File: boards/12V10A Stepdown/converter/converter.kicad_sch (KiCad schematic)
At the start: 27 parts, among them IC1 CSD17578Q3A, J1 TB005-762-02BE, J2 TB005-762-02BE, Q1 CSD17571Q2, U1 LM25145RGYR

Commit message: Whoops didn't save
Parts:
- 2.2uH: value L -> L1; footprint (none) -> 10A_LIbrary:IND_XAL7070_COC
- Cbst, Cvin: footprint (none) -> 10A_LIbrary:CAP_1608_TDK
- Ccomp1, Ccomp2, Css: footprint (none) -> 10A_LIbrary:G-155_MUR
- Ccomp3: footprint (none) -> 10A_LIbrary:CAPC1005X55N
- Cilim, Cvcc, Rvcc: footprint (none) -> 10A_LIbrary:CAP_06031U0R5BAT2A
- Cin: footprint (none) -> 10A_LIbrary:CAP_MSAS32-M_TAY
- Cout: footprint (none) -> 10A_LIbrary:PCAP_SVP_B6_PAN
- M1: renamed from IC1; footprint CSD17578Q3A:TRANS_CSD18543Q3A -> 10A_LIbrary:DNH0008A
- M2: renamed from Q1; footprint CSD17571Q2:TRANS_CSD17571Q2 -> 10A_LIbrary:DQK0006C
- Rcomp2, Rfbb, Ruv1, Rvin: footprint (none) -> 10A_LIbrary:RC0402N_VIS
- Rfbt, Rpgood: footprint (none) -> 10A_LIbrary:RC0603N_YAG
- Rilim, Rt: footprint (none) -> 10A_LIbrary:RES_CRCW_0402
- Ruv2: footprint (none) -> 10A_LIbrary:RES_CRCW_0603
- U1: footprint LM25145RGYR:IC_LM25145RGYR -> 10A_LIbrary:RGY0020B
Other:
- moved on the sheet: 2.2uH, Cbst, Ccomp1, Ccomp2, Ccomp3, Cilim, Cin, Cout, Css, Cvcc, Cvin, J1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

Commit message: PCB schematic done with footprints
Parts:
- J1, J2: footprint TB005-762-02BE:CUI_TB005-762-02BE -> 10A_LIbrary:TB005-762-02BE_CUD
- Rcomp1: footprint (none) -> 10A_LIbrary:RES_CRCW_0402
- renumbered 2.2uH to 2.2uH1, Cbst to Cbst1, Cilim to Cilim1, Cin to Cin1, Cout to Cout1, Css to Css1, Cvcc to Cvcc1, Cvin to Cvin1, Rfbb to Rfbb1, Rfbt to Rfbt1, Rilim to Rilim1, Rpgood to Rpgood1, Rt to Rt1, Rvcc to Rvcc1, Rvin to Rvin1
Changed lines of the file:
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@@
 		(dnp no)
 		(fields_autoplaced yes)
-		(property "Reference" "Cilim"
+		(property "Reference" "Cilim1"
 			(at 162.56 120.6499 0)
 			(effects
@@
 			(project "converter"
 				(path "/1513ce43-e5f2-482b-99a2-cdd75b9aa1c1"
-					(reference "Cilim")
+					(reference "Cilim1")
 					(unit 1)
 				)
@@
 			)
 		)
-		(property "Footprint" ""
+		(property "Footprint" "10A_LIbrary:RES_CRCW_0402"
 			(at 189.484 82.804 90)
 			(effects
@@
 		(dnp no)
 		(fields_autoplaced yes)
-		(property "Reference" "Rfbb"
+		(property "Reference" "Rfbb1"
 			(at 214.63 130.8099 0)
 			(effects
@@
 			(project "converter"
 				(path "/1513ce43-e5f2-482b-99a2-cdd75b9aa1c1"
-					(reference "Rfbb")
+					(reference "Rfbb1")
 					(unit 1)
 				)
@@
 		(dnp no)
 		(fields_autoplaced yes)
-		(property "Reference" "Cvin"
+		(property "Reference" "Cvin1"
 			(at 82.55 69.8499 0)
 			(effects
@@
 			(project "converter"
 				(path "/1513ce43-e5f2-482b-99a2-cdd75b9aa1c1"
-					(reference "Cvin")
+					(reference "Cvin1")
 					(unit 1)
 				)
@@
 			)
 		)
-		(property "Footprint" "TB005-762-02BE:CUI_TB005-762-02BE"
+		(property "Footprint" "10A_LIbrary:TB005-762-02BE_CUD"
 			(at 252.73 114.3 0)
 			(effects
@@
 		(dnp no)
 		(fields_autoplaced yes)
-		(property "Reference" "Rpgood"
+		(property "Reference" "Rpgood1"
 			(at 139.7 99.0599 0)
 			(effects
@@
 			(project "converter"
 				(path "/1513ce43-e5f2-482b-99a2-cdd75b9aa1c1"
-					(reference "Rpgood")
+					(reference "Rpgood1")
 					(unit 1)
 				)
@@
 		(dnp no)
 		(fields_autoplaced yes)
-		(property "Reference" "2.2uH"
+		(property "Reference" "2.2uH1"
 			(at 168.91 90.17 90)
 			(effects
@@
 			(project "converter"
 				(path "/1513ce43-e5f2-482b-99a2-cdd75b9aa1c1"
-					(reference "2.2uH")
+					(reference "2.2uH1")
 					(unit 1)
 				)
@@
 		(dnp no)
 		(fields_autoplaced yes)
-		(property "Reference" "Cin"
+		(property "Reference" "Cin1"
 			(at 52.07 76.1999 0)
 			(effects
@@
 			(project "converter"
 				(path "/1513ce43-e5f2-482b-99a2-cdd75b9aa1c1"
-					(reference "Cin")
+					(reference "Cin1")
 					(unit 1)
 				)
@@
 		(dnp no)
 		(fields_autoplaced yes)
-		(property "Reference" "Rt"
+		(property "Reference" "Rt1"
 			(at 62.23 104.1399 0)
 			(effects
@@
 			(project "converter"
 				(path "/1513ce43-e5f2-482b-99a2-cdd75b9aa1c1"
-					(reference "Rt")
+					(reference "Rt1")
 					(unit 1)
 				)
@@
 		(dnp no)
 		(fields_autoplaced yes)
-		(property "Reference" "Cvcc"
+		(property "Reference" "Cvcc1"
 			(at 147.32 120.6499 0)
 			(effects
@@
 			(project "converter"
 				(path "/1513ce43-e5f2-482b-99a2-cdd75b9aa1c1"
-					(reference "Cvcc")
+					(reference "Cvcc1")
 					(unit 1)
 				)
@@
 		(dnp no)
 		(fields_autoplaced yes)
-		(property "Reference" "Css"
+		(property "Reference" "Css1"
 			(at 74.93 104.1399 0)
 			(effects
@@
 			(project "converter"
 				(path "/1513ce43-e5f2-482b-99a2-cdd75b9aa1c1"
-					(reference "Css")
+					(reference "Css1")
 					(unit 1)
 				)
@@
 		(dnp no)
 		(fields_autoplaced yes)
-		(property "Reference" "Cout"
+		(property "Reference" "Cout1"
 			(at 234.95 106.2481 0)
 			(effects
@@
 			(project "converter"
 				(path "/1513ce43-e5f2-482b-99a2-cdd75b9aa1c1"
-					(reference "Cout")
+					(reference "Cout1")
 					(unit 1)
 				)
@@
 		(dnp no)
 		(fields_autoplaced yes)
-		(property "Reference" "Rvin"
+		(property "Reference" "Rvin1"
 			(at 81.28 52.0699 0)
 			(effects
@@
 			(project "converter"
 				(path "/1513ce43-e5f2-482b-99a2-cdd75b9aa1c1"
-					(reference "Rvin")
+					(reference "Rvin1")
 					(unit 1)
 				)
@@
 		(dnp no)
 		(fields_autoplaced yes)
-		(property "Reference" "Rvcc"
+		(property "Reference" "Rvcc1"
 			(at 152.4 99.0599 0)
 			(effects
@@
 			(project "converter"
 				(path "/1513ce43-e5f2-482b-99a2-cdd75b9aa1c1"
-					(reference "Rvcc")
+					(reference "Rvcc1")
 					(unit 1)
 				)
@@
 		(dnp no)
 		(fields_autoplaced yes)
-		(property "Reference" "Cbst"
+		(property "Reference" "Cbst1"
 			(at 134.62 81.28 90)
 			(effects
@@
 			(project "converter"
 				(path "/1513ce43-e5f2-482b-99a2-cdd75b9aa1c1"
-					(reference "Cbst")
+					(reference "Cbst1")
 					(unit 1)
 				)
@@
 			)
 		)
-		(property "Footprint" "TB005-762-02BE:CUI_TB005-762-02BE"
+		(property "Footprint" "10A_LIbrary:TB005-762-02BE_CUD"
 			(at 39.37 60.96 0)
 			(effects
@@
 		(dnp no)
 		(fields_autoplaced yes)
-		(property "Reference" "Rfbt"
+		(property "Reference" "Rfbt1"
 			(at 214.63 100.3299 0)
 			(effects
@@
 			(project "converter"
 				(path "/1513ce43-e5f2-482b-99a2-cdd75b9aa1c1"
-					(reference "Rfbt")
+					(reference "Rfbt1")
 					(unit 1)
 				)
@@
 		(on_board yes)
 		(dnp no)
-		(property "Reference" "Rilim"
+		(property "Reference" "Rilim1"
 			(at 165.1 82.5499 0)
 			(effects
@@
 			(project "converter"
 				(path "/1513ce43-e5f2-482b-99a2-cdd75b9aa1c1"
-					(reference "Rilim")
-					(unit 1)
-				)
+					(reference "Rilim1")
+					(unit 1)
+				)

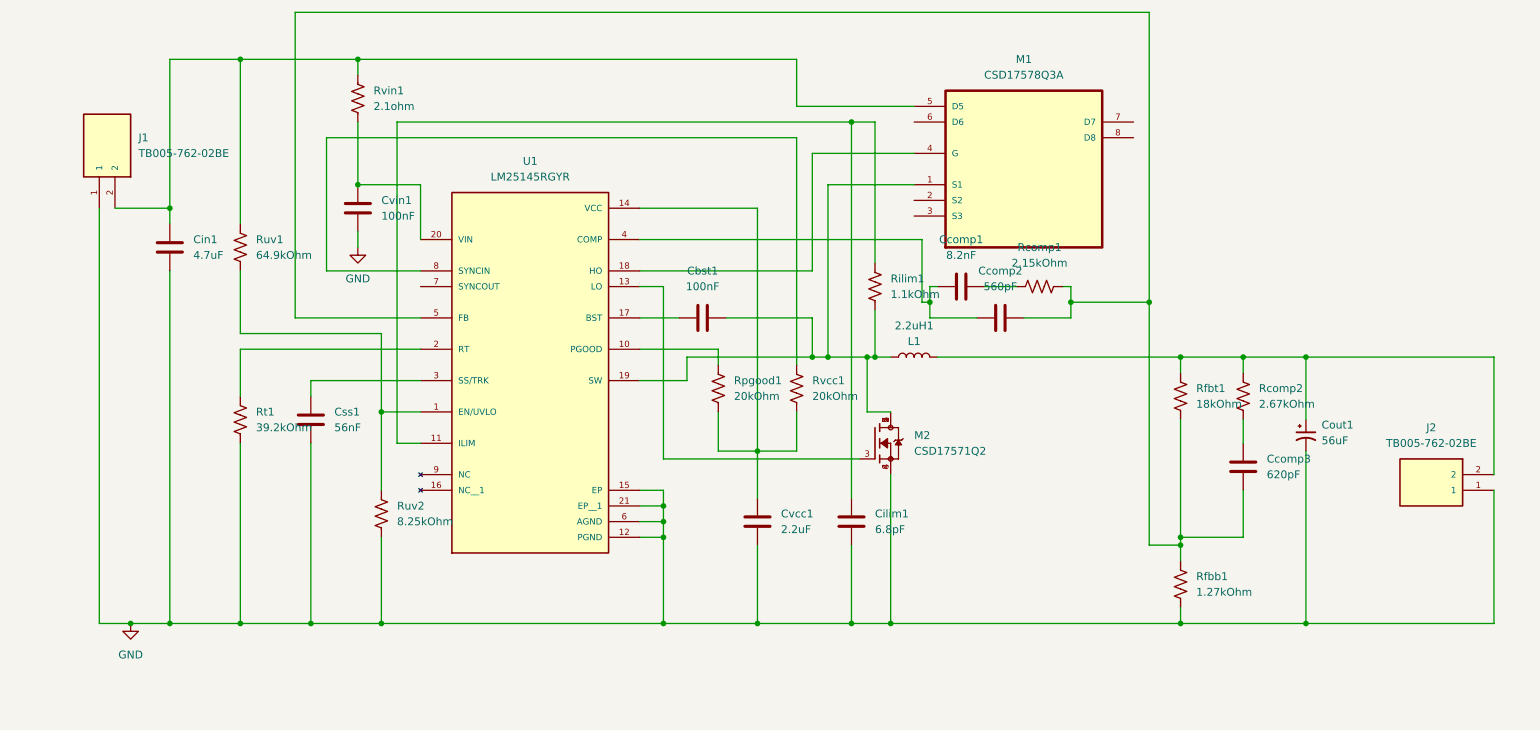
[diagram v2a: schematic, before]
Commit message: iris silkscreen stuff for 20a board
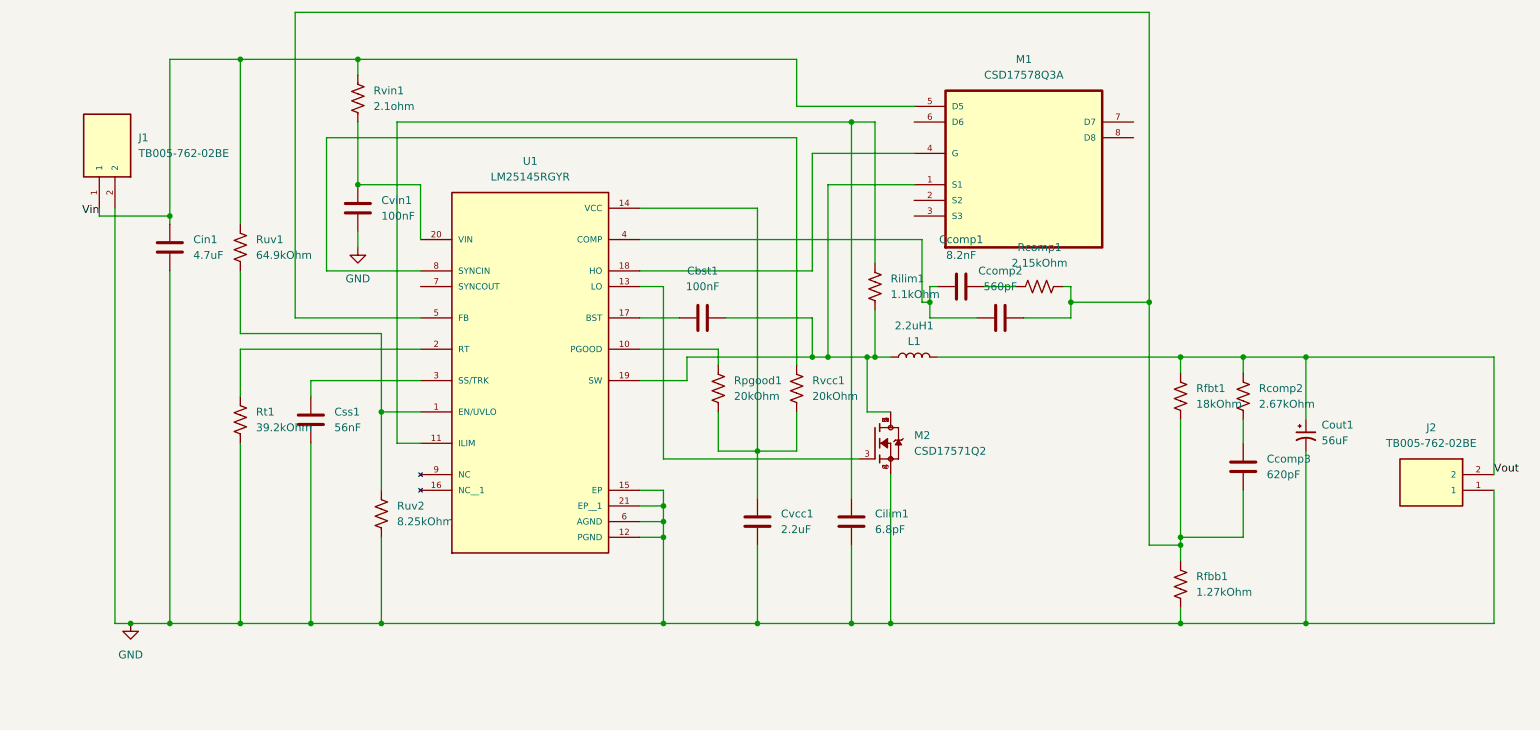
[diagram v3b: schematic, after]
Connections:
- net GND: now also J1.2; no longer J1.1
- net Vin: now reaches Cin1.1, M1.5 (D5), Ruv1.1, Rvin1.1
- net Vin: now also J1.1; no longer J1.2
- net Vout: now reaches 2.2uH1.2, Cout1.1, J2.2, Rcomp2.1, Rfbt1.1
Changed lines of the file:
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@@
-	)
-	(junction
-		(at 48.26 71.12)
-		(diameter 0)
-		(color 0 0 0 0)
 	)
 	(junction
@@
 	)
 	(junction
+		(at 48.26 72.39)
+		(diameter 0)
+		(color 0 0 0 0)
+	)
+	(junction
 		(at 71.12 138.43)
 		(diameter 0)
@@
 	(wire
 		(pts
-			(xy 36.83 71.12) (xy 36.83 138.43)
-		)
-		(stroke
-			(width 0)
-			(type default)
-		)
-	)
-	(wire
-		(pts
 			(xy 132.08 99.06) (xy 132.08 95.25)
 		)
@@
 	(wire
 		(pts
-			(xy 39.37 71.12) (xy 48.26 71.12)
-		)
-		(stroke
-			(width 0)
-			(type default)
-		)
-	)
-	(wire
-		(pts
 			(xy 207.01 39.37) (xy 207.01 86.36)
 		)
@@
 	(wire
 		(pts
-			(xy 48.26 46.99) (xy 48.26 71.12)
+			(xy 48.26 46.99) (xy 48.26 72.39)
+		)
+		(stroke
+			(width 0)
+			(type default)
+		)
+	)
+	(wire
+		(pts
+			(xy 36.83 71.12) (xy 36.83 72.39)
 		)
 		(stroke
@@
 	(wire
 		(pts
+			(xy 36.83 72.39) (xy 48.26 72.39)
+		)
+		(stroke
+			(width 0)
+			(type default)
+		)
+	)
+	(wire
+		(pts
 			(xy 82.55 91.44) (xy 82.55 104.14)
 		)
@@
 	(wire
 		(pts
+			(xy 39.37 71.12) (xy 39.37 138.43)
+		)
+		(stroke
+			(width 0)
+			(type default)
+		)
+	)
+	(wire
+		(pts
 			(xy 78.74 46.99) (xy 149.86 46.99)
 		)
@@
 	(wire
 		(pts
-			(xy 36.83 138.43) (xy 41.91 138.43)
-		)
-		(stroke
-			(width 0)
-			(type default)
-		)
-	)
-	(wire
-		(pts
 			(xy 207.01 86.36) (xy 207.01 125.73)
 		)
@@
 	(wire
 		(pts
-			(xy 48.26 71.12) (xy 48.26 73.66)
-		)
-		(stroke
-			(width 0)
-			(type default)
-		)
-	)
-	(wire
-		(pts
 			(xy 85.09 57.15) (xy 158.75 57.15)
 		)
@@
 	(wire
 		(pts
+			(xy 48.26 72.39) (xy 48.26 73.66)
+		)
+		(stroke
+			(width 0)
+			(type default)
+		)
+	)
+	(wire
+		(pts
 			(xy 78.74 46.99) (xy 59.69 46.99)
 		)
@@
 	(wire
 		(pts
+			(xy 39.37 138.43) (xy 41.91 138.43)
+		)
+		(stroke
+			(width 0)
+			(type default)
+		)
+	)
+	(wire
+		(pts
 			(xy 212.09 124.46) (xy 222.25 124.46)
 		)
@@
 		)
 	)
+	(label "Vout"
+		(at 262.89 114.3 0)
+		(effects
+			(font
+				(size 1.27 1.27)
+			)
+			(justify left bottom)
+		)
+	)
+	(label "Vin"
+		(at 36.83 72.39 180)
+		(effects
+			(font
+				(size 1.27 1.27)
+			)
+			(justify right bottom)
+		)
+	)

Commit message: minor fixes
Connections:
- net GND: now also U1.V (EP_V)
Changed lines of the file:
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@@
+	)
+	(junction
+		(at 88.9 138.43)
+		(diameter 0)
+		(color 0 0 0 0)
 	)
 	(junction
@@
 	(wire
 		(pts
+			(xy 91.44 124.46) (xy 88.9 124.46)
+		)
+		(stroke
+			(width 0)
+			(type default)
+		)
+	)
+	(wire
+		(pts
 			(xy 207.01 39.37) (xy 207.01 86.36)
 		)
@@
 	(wire
 		(pts
-			(xy 82.55 138.43) (xy 128.27 138.43)
+			(xy 82.55 138.43) (xy 88.9 138.43)
 		)
 		(stroke
@@
 	(wire
 		(pts
+			(xy 88.9 124.46) (xy 88.9 138.43)
+		)
+		(stroke
+			(width 0)
+			(type default)
+		)
+	)
+	(wire
+		(pts
 			(xy 172.72 83.82) (xy 171.45 83.82)
 		)
@@
 		(pts
 			(xy 124.46 124.46) (xy 128.27 124.46)
+		)
+		(stroke
+			(width 0)
+			(type default)
+		)
+	)
+	(wire
+		(pts
+			(xy 88.9 138.43) (xy 128.27 138.43)
 		)
 		(stroke
@@
 		(pin "21"
 		)
+		(pin "V"
+		)
 		(instances

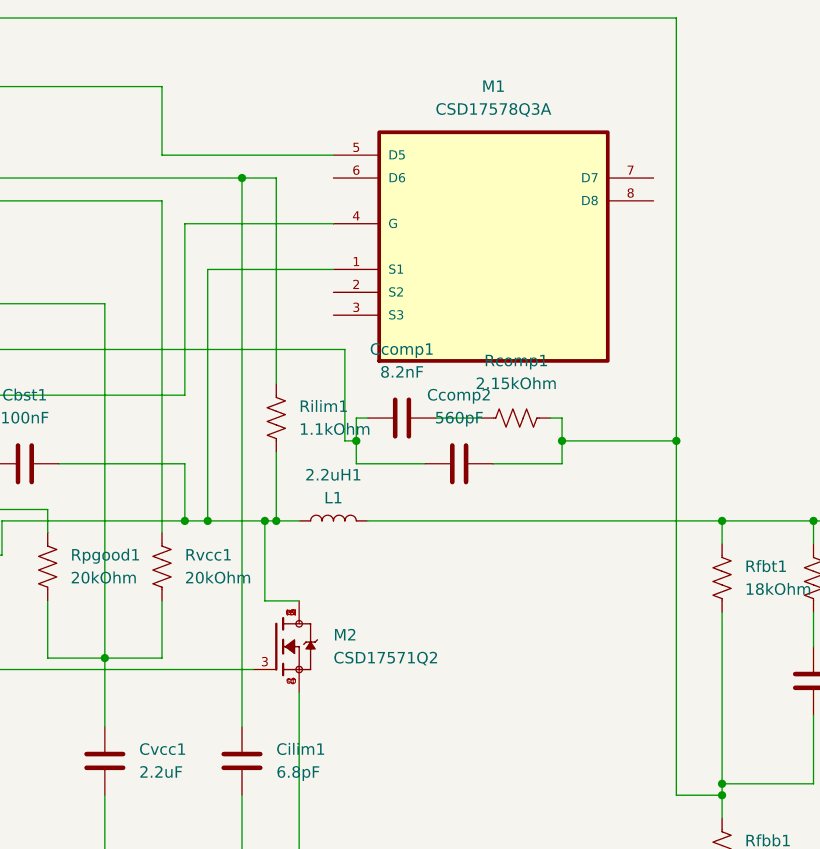
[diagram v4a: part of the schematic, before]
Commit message: 10a stepdown and 20a stepdown update
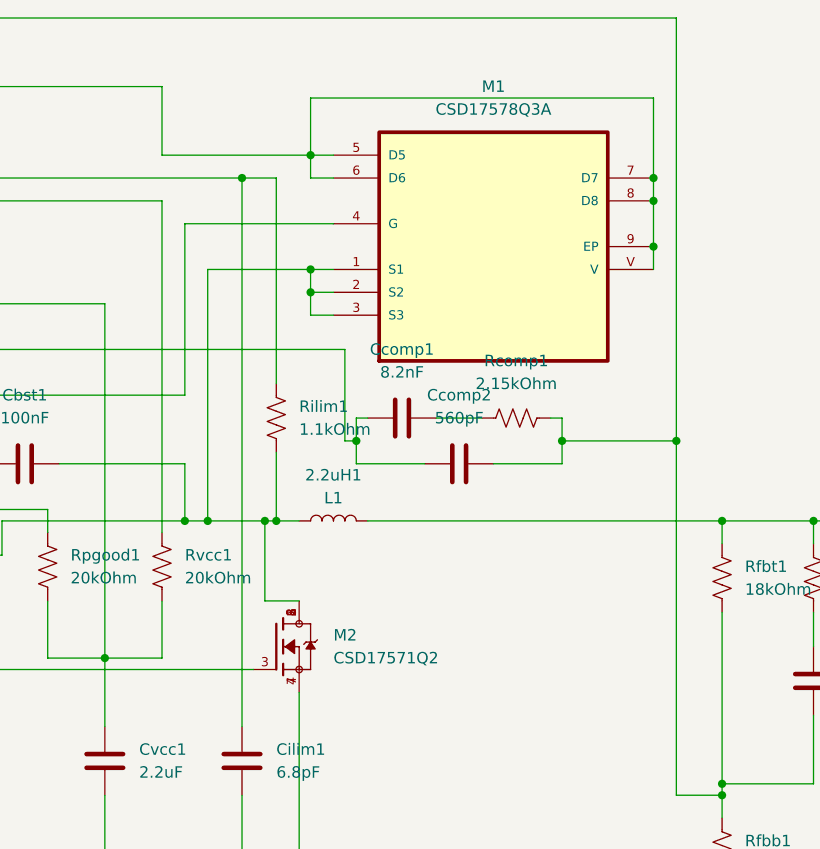
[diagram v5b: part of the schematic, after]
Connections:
- net GND: now also M2.7; no longer M2.8
- net Vin: now also M1.6 (D6), M1.7 (D7), M1.8 (D8), M1.9 (EP), M1.V
- net at 2.2uH1.1, Cbst1.2, M1.1 (S1)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: now also M1.2 (S2), M1.3 (S3), M2.8; no longer M2.7
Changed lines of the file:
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@@
 	)
 	(junction
+		(at 204.47 57.15)
+		(diameter 0)
+		(color 0 0 0 0)
+	)
+	(junction
+		(at 166.37 54.61)
+		(diameter 0)
+		(color 0 0 0 0)
+	)
+	(junction
 		(at 143.51 138.43)
 		(diameter 0)
@@
 	)
 	(junction
+		(at 166.37 67.31)
+		(diameter 0)
+		(color 0 0 0 0)
+	)
+	(junction
 		(at 48.26 138.43)
 		(diameter 0)
@@
 	)
 	(junction
+		(at 204.47 59.69)
+		(diameter 0)
+		(color 0 0 0 0)
+	)
+	(junction
 		(at 171.45 86.36)
 		(diameter 0)
@@
 	)
 	(junction
+		(at 166.37 69.85)
+		(diameter 0)
+		(color 0 0 0 0)
+	)
+	(junction
 		(at 212.09 95.25)
 		(diameter 0)
@@
 	)
 	(junction
+		(at 204.47 64.77)
+		(diameter 0)
+		(color 0 0 0 0)
+	)
+	(junction
 		(at 222.25 95.25)
 		(diameter 0)
@@
 	(wire
 		(pts
-			(xy 149.86 54.61) (xy 168.91 54.61)
+			(xy 59.69 138.43) (xy 71.12 138.43)
 		)
 		(stroke
@@
 	(wire
 		(pts
-			(xy 59.69 138.43) (xy 71.12 138.43)
+			(xy 128.27 121.92) (xy 128.27 124.46)
 		)
 		(stroke
@@
 	(wire
 		(pts
-			(xy 128.27 121.92) (xy 128.27 124.46)
+			(xy 166.37 72.39) (xy 168.91 72.39)
 		)
 		(stroke
@@
 	(wire
 		(pts
+			(xy 204.47 64.77) (xy 204.47 67.31)
+		)
+		(stroke
+			(width 0)
+			(type default)
+		)
+	)
+	(wire
+		(pts
+			(xy 204.47 57.15) (xy 204.47 48.26)
+		)
+		(stroke
+			(width 0)
+			(type default)
+		)
+	)
+	(wire
+		(pts
 			(xy 91.44 124.46) (xy 88.9 124.46)
 		)
@@
 	(wire
 		(pts
+			(xy 168.91 57.15) (xy 166.37 57.15)
+		)
+		(stroke
+			(width 0)
+			(type default)
+		)
+	)
+	(wire
+		(pts
 			(xy 71.12 138.43) (xy 82.55 138.43)
 		)
@@
 	(wire
 		(pts
+			(xy 166.37 54.61) (xy 168.91 54.61)
+		)
+		(stroke
+			(width 0)
+			(type default)
+		)
+	)
+	(wire
+		(pts
 			(xy 48.26 46.99) (xy 48.26 72.39)
 		)
@@
 	(wire
 		(pts
+			(xy 166.37 48.26) (xy 166.37 54.61)
+		)
+		(stroke
+			(width 0)
+			(type default)
+		)
+	)
+	(wire
+		(pts
 			(xy 124.46 116.84) (xy 128.27 116.84)
 		)
@@
 	(wire
 		(pts
-			(xy 168.91 67.31) (xy 154.94 67.31)
+			(xy 168.91 67.31) (xy 166.37 67.31)
+		)
+		(stroke
+			(width 0)
+			(type default)
+		)
+	)
+	(wire
+		(pts
+			(xy 166.37 69.85) (xy 168.91 69.85)
+		)
+		(stroke
+			(width 0)
+			(type default)
+		)
+	)
+	(wire
+		(pts
+			(xy 149.86 54.61) (xy 166.37 54.61)
 		)
 		(stroke
@@
 	(wire
 		(pts
+			(xy 166.37 57.15) (xy 166.37 54.61)
+		)
+		(stroke
+			(width 0)
+			(type default)
+		)
+	)
+	(wire
+		(pts
 			(xy 194.31 86.36) (xy 194.31 88.9)
 		)
@@
 	(wire
 		(pts
+			(xy 166.37 67.31) (xy 166.37 69.85)
+		)
+		(stroke
+			(width 0)
+			(type default)
+		)
+	)
+	(wire
+		(pts
 			(xy 162.56 87.63) (xy 162.56 95.25)
 		)
@@
 	(wire
 		(pts
+			(xy 204.47 48.26) (xy 166.37 48.26)
+		)
+		(stroke
+			(width 0)
+			(type default)
+		)
+	)
+	(wire
+		(pts
 			(xy 124.46 76.2) (xy 170.18 76.2)
 		)
@@
 	(wire
 		(pts
+			(xy 204.47 57.15) (xy 204.47 59.69)
+		)
+		(stroke
+			(width 0)
+			(type default)
+		)
+	)
+	(wire
+		(pts
 			(xy 161.29 104.14) (xy 165.1 104.14)
 		)
@@
 	(wire
 		(pts
+			(xy 204.47 59.69) (xy 204.47 64.77)
+		)
+		(stroke
+			(width 0)
+			(type default)
+		)
+	)
+	(wire
+		(pts
 			(xy 212.09 124.46) (xy 222.25 124.46)
 		)
@@
 	(wire
 		(pts
+			(xy 166.37 69.85) (xy 166.37 72.39)
+		)
+		(stroke
+			(width 0)
+			(type default)
+		)
+	)
+	(wire
+		(pts
+			(xy 166.37 67.31) (xy 154.94 67.31)
+		)
+		(stroke
+			(width 0)
+			(type default)
+		)
+	)
+	(wire
+		(pts
 			(xy 73.66 59.69) (xy 149.86 59.69)
 		)
@@
 		(pin "7"
 		)
+		(pin "9"
+		)
+		(pin "V"
+		)
 		(instances
